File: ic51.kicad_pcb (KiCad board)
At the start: 2 copper layers, 5 parts, among them J1 Conn_02x18_Odd_Even, J2 Conn_02x18_Odd_Even, J3 Conn_02x18_Odd_Even, J4 Conn_02x18_Odd_Even, U1 ic51-1444-schem

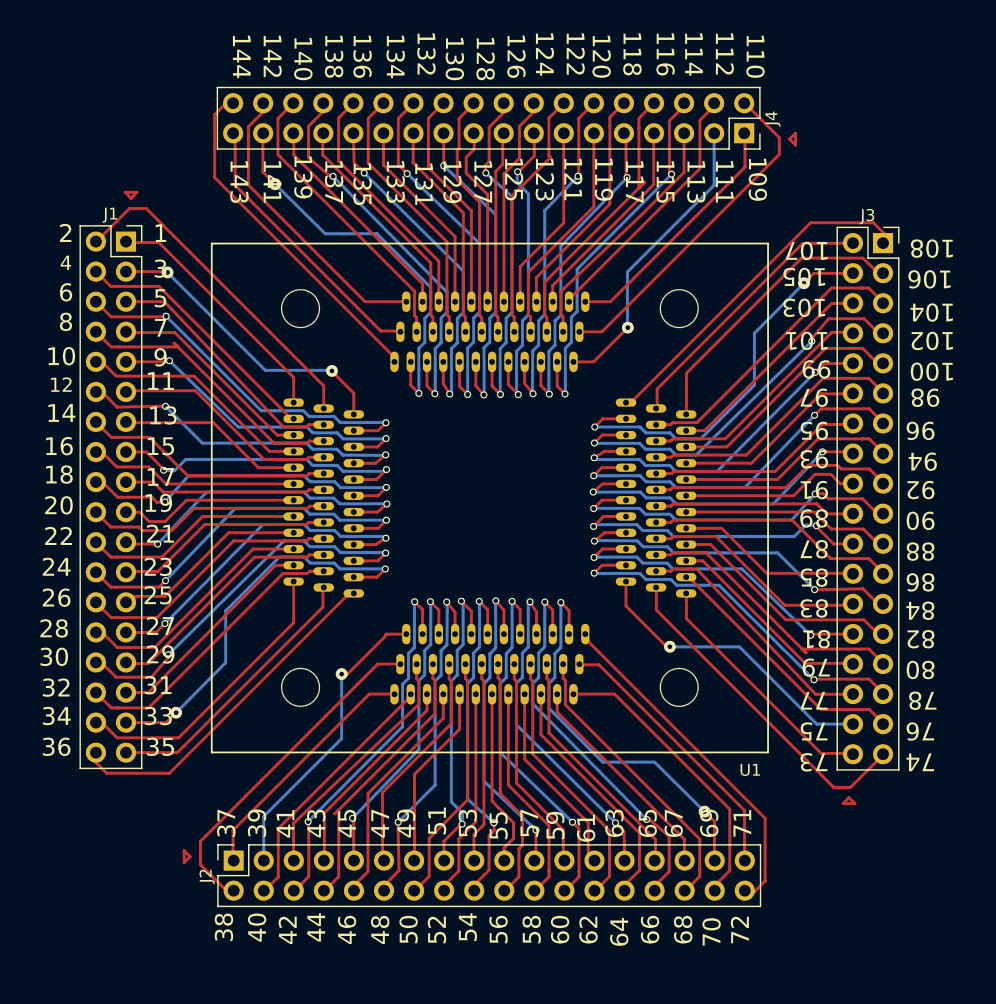
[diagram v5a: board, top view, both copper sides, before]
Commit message: decrease font size of text in F.silk layer
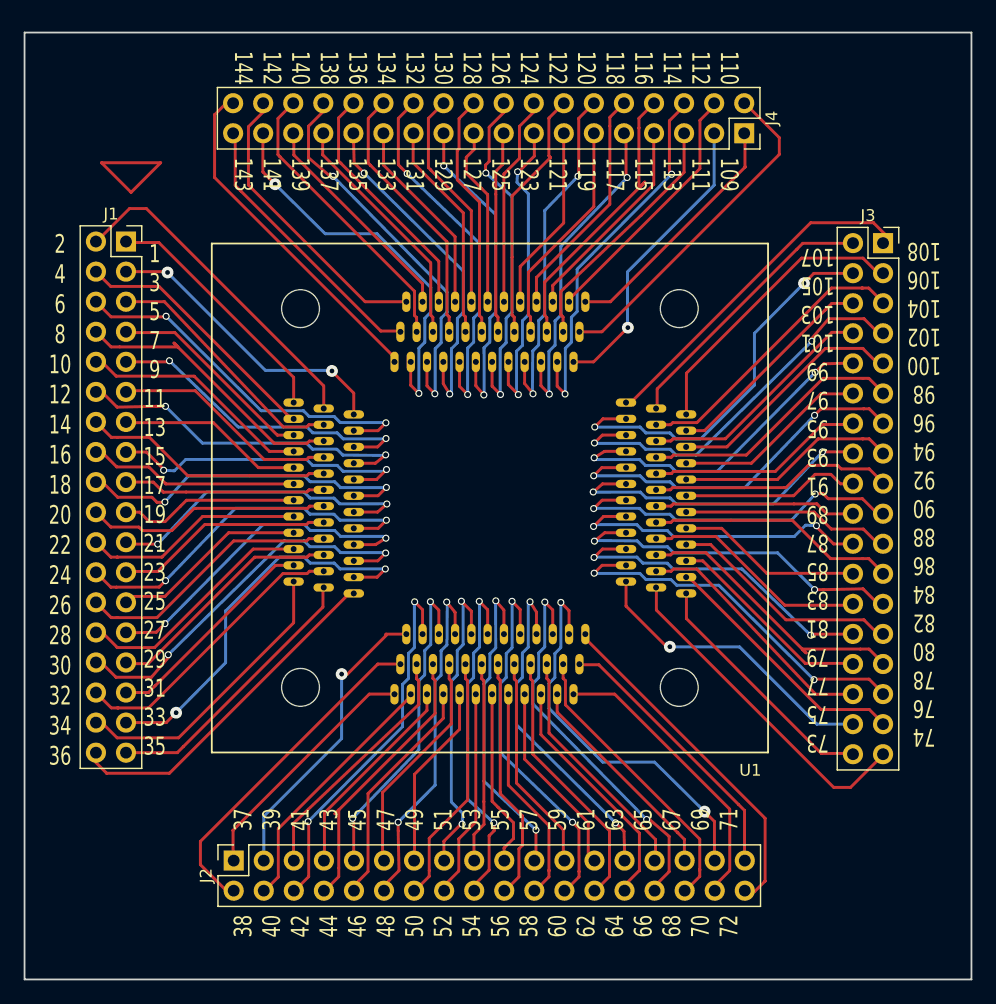
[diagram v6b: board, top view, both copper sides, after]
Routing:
- net (no net): track 9.66 -> 12.1 mm
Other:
- board outline added: 80 x 80 mm
- board text added: "1 3 5 7 9 11 13 15 17 19 21 23 25 27 29 31 33 35"
- board text added: "109 111 113 115 117 119 121 123 125 127 129 131 133 135 137 139 141 143"
- board text added: "110 112 114 116 118 120 122 124 126 128 130 132 134 136 138 140 142 144"
- board text added: "2 4 6 8 10 12 14 16 18 20 22 24 26 28 30 32 34 36"
- board text added: "37 39 41 43 45 47 49 51 53 55 57 59 61 63 65 67 69 71"
- board text added: "38 40 42 44 46 48 50 52 54 56 58 60 62 64 66 68 70 72"
- board text added: "73 75 77 79 81 83 85 87 89 91 93 95 97 99 101 103 105 107"
- board text added: "74 76 78 80 82 84 86 88 90 92 94 96 98 100 102 104 106 108"
- board text removed: "1"
- board text removed: "10"
- board text removed: "100"
- board text removed: "101"
- board text removed: "102"
- board text removed: "103"
- board text removed: "104"
- board text removed: "105"
- board text removed: "106"
- board text removed: "107"
- board text removed: "108"
- board text removed: "109"
- board text removed: "11"
- board text removed: "110"
- board text removed: "111"
- board text removed: "112"
- board text removed: "113"
- board text removed: "114"
- board text removed: "115"
- board text removed: "116"
- board text removed: "117"
- board text removed: "118"
- board text removed: "119"
- board text removed: "12"
- board text removed: "120"
- board text removed: "121"
- board text removed: "122"
- board text removed: "123"
- board text removed: "124"
- board text removed: "125"
- board text removed: "126"
- board text removed: "127"
- board text removed: "128"
- board text removed: "129"
- board text removed: "13"
- board text removed: "130"
- board text removed: "131"
- board text removed: "132"
- board text removed: "133"
- board text removed: "134"
- board text removed: "135"
- board text removed: "136"
- board text removed: "137"
- board text removed: "138"
- board text removed: "139"
- board text removed: "14"
- board text removed: "140"
- board text removed: "141"
- board text removed: "142"
- board text removed: "143"
- board text removed: "144"
- board text removed: "15"
- board text removed: "16"
- board text removed: "17"
- board text removed: "18"
- board text removed: "19"
- board text removed: "2"
- board text removed: "20"
- board text removed: "21"
- board text removed: "22"
- board text removed: "23"
- board text removed: "24"
- board text removed: "25"
- board text removed: "26"
- board text removed: "27"
- board text removed: "28"
- board text removed: "29"
- board text removed: "3"
- board text removed: "30"
- board text removed: "31"
- board text removed: "32"
- board text removed: "33"
- board text removed: "34"
- board text removed: "35"
- board text removed: "36"
- board text removed: "37"
- board text removed: "38"
- board text removed: "39"
- board text removed: "4"
- board text removed: "40"
- board text removed: "41"
- board text removed: "42"
- board text removed: "43"
- board text removed: "44"
- board text removed: "45"
- board text removed: "46"
- board text removed: "47"
- board text removed: "48"
- board text removed: "49"
- board text removed: "5"
- board text removed: "50"
- board text removed: "51"
- board text removed: "52"
- board text removed: "53"
- board text removed: "54"
- board text removed: "55"
- board text removed: "56"
- board text removed: "57"
- board text removed: "58"
- board text removed: "59"
- board text removed: "6"
- board text removed: "60"
- board text removed: "61"
- board text removed: "62"
- board text removed: "63"
- board text removed: "64"
- board text removed: "65"
- board text removed: "66"
- board text removed: "67"
- board text removed: "68"
- board text removed: "69"
- board text removed: "7"
- board text removed: "70"
- board text removed: "71"
- board text removed: "72"
- board text removed: "73"
- board text removed: "74"
- board text removed: "75"
- board text removed: "76"
- board text removed: "77"
- board text removed: "78"
- board text removed: "79"
- board text removed: "8"
- board text removed: "80"
- board text removed: "81"
- board text removed: "82"
- board text removed: "83"
- board text removed: "84"
- board text removed: "85"
- board text removed: "86"
- board text removed: "87"
- board text removed: "88"
- board text removed: "89"
- board text removed: "9"
- board text removed: "90"
- board text removed: "91"
- board text removed: "92"
- board text removed: "93"
- board text removed: "94"
- board text removed: "95"
- board text removed: "96"
- board text removed: "97"
- board text removed: "98"
- board text removed: "99"

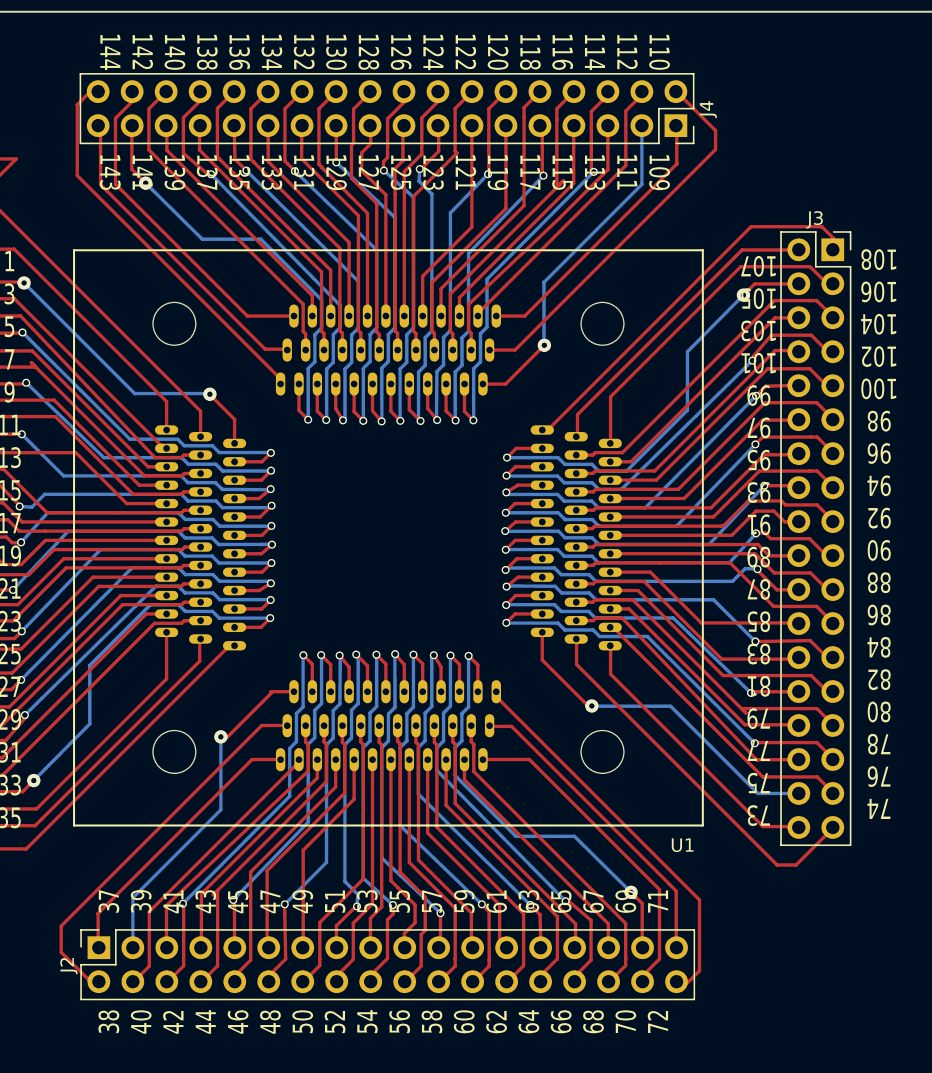
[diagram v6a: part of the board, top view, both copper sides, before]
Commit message: remove square at first pin except pin 1
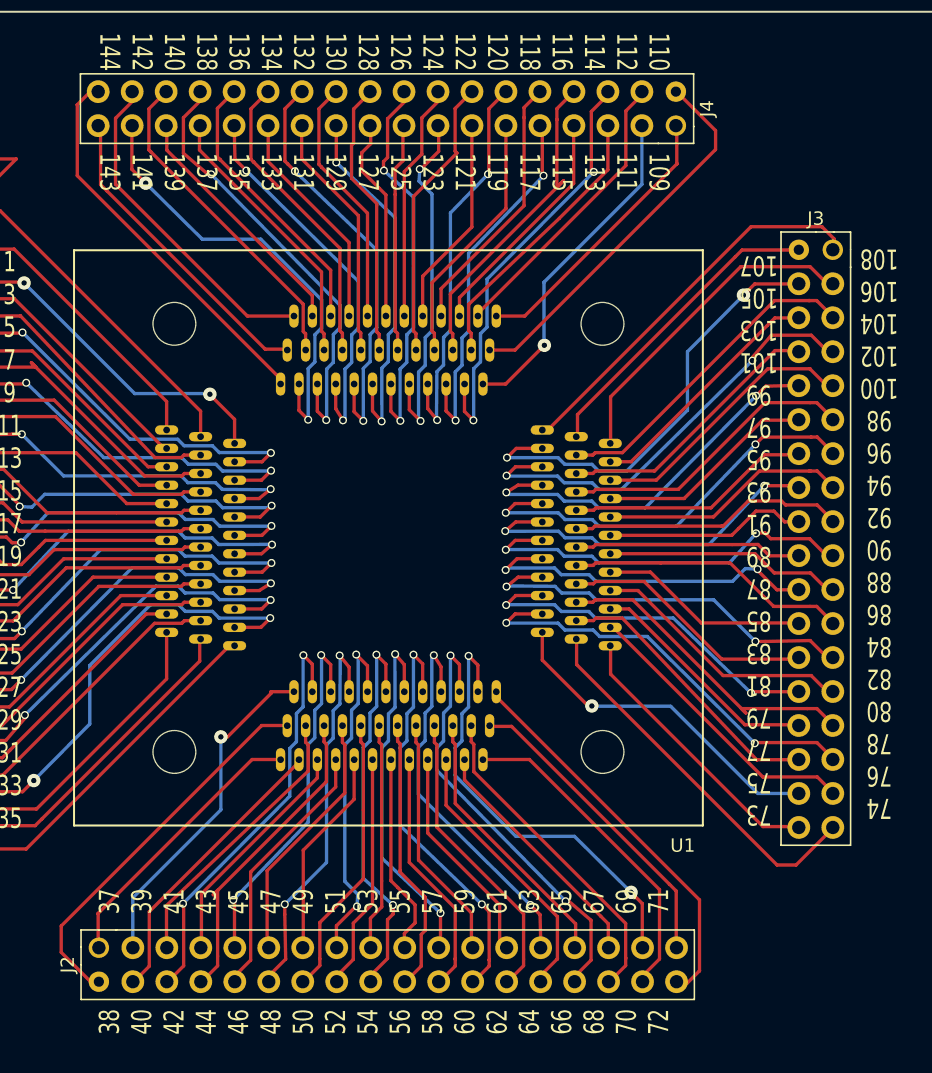
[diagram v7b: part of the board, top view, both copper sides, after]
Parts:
- J2, J3, J4: footprint Socket_Strips:Socket_Strip_Straight_2x18_Pitch2.54mm -> ic51-1444:Socket_Strip_Straight_2x18_Pitch2.54mm_no_rectangle

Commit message: move pin header closer
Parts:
- moved J4 1.57 mm to (167.8, 64.6)
- moved J1 1.50 mm to (117.1, 72.2)
- moved J3 1.43 mm to (178.1, 72.3)
- moved J2 1.34 mm to (124.7, 123.1)
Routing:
- net /69: track 33.7 -> 65.0 mm, vias 2 -> 4
- net /66: track 33.3 -> 63.7 mm, vias 2 -> 4
- net /42: track 32.0 -> 61.0 mm, vias 2 -> 4
- net /60: track 31.3 -> 59.7 mm, vias 2 -> 4
- net /54: track 29.9 -> 56.3 mm, vias 2 -> 4
- net /48: track 29.9 -> 56.3 mm, vias 2 -> 4
- net /63: track 29.2 -> 55.1 mm, vias 2 -> 4
- net /72: track 29.8 -> 55.7 mm
- net /45: track 27.7 -> 52.6 mm, vias 2 -> 4
- net /57: track 27.6 -> 52.4 mm, vias 2 -> 4
- net /51: track 26.7 -> 50.9 mm, vias 2 -> 4
- net /38: track 28.8 -> 52.9 mm
- net /39: track 25.4 -> 48.0 mm, vias 1 -> 4
- net /74: track 28.6 -> 51.0 mm
- net /70: track 24.7 -> 46.5 mm
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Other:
- board text added: "1"
